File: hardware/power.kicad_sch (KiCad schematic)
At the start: 26 parts, among them J2 +, J3 -, U1 INA186A3, U2 TPS61022, U4 LP5912-3.3

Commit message: Preserve owner schematic and board before final design review
Snapshot of the saved working design supplied for review.
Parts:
- removed C1, C2: 22uF, lib:C_0603_1608Metric_L, symbol Device:C
- removed R1: 0.5mR 2W, lib:R_1206_Kelvin_4Pad_NetTie_HCS1206_L, symbol lib:R_Shunt_Kelvin
- added R2: 0.5mR 2W, lib:R_1206_Kelvin_4Pad_NetTie_HCS1206_L, symbol lib:R_Shunt_Kelvin
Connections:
- net +BATT: now also R2.4
- net CSA+: now also R2.1
- net SHUNT_SENSE_N: now also R2.3
- net SHUNT_SENSE_P: now also R2.2

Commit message: Correct Whoop schematic and prepare component library for routing
Add local BMI270 bypassing, improve regulator capacitance margin, isolate
bidirectional DShot supply domains, and correct PA reference accuracy.
Remove Q28/R11 with matching firmware polarity and retain the proven
OpenFC-Lite OSD topology. Correct the receiver LED bypass rail.

Synchronize PCB connectivity, verify component pins and land patterns,
and provide firmware bindings plus placement/layer guidance. Replace stale
manual BOM and interface plans with schematic-derived exports.

Validation: ERC 0, seven netlist checks, 48 footprint checks, 22 rule
behavior cases, and PCB schematic parity 0. The parked PCB retains layout
DRC findings and 499 unconnected items; no manufacturing or flight release.
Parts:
- removed R11: 2.4k, lib:R_0201_0603Metric_L, symbol Device:R
- added D11: MS2A40LDF, lib:DFN1610-2_L1.6-W1.0-P1.05-RD, symbol lib:MS2A40LDF
- C14: value 1uF -> 4.7uF; LCSC C76935 -> C335103; MPN GRM033R61A105ME44D -> GRM035R60J475ME15D
- U4: value LP5912-3.3 -> TLV75733; symbol lib:LP5912-3.3DRVR -> lib:TLV75733PDRVR; LCSC C524780 -> C2868428; MPN LP5912-3.3DRVR -> TLV75733PDRVR
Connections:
- net +3.3V: now also D11.2 (A)
- net +5V: now also D11.1 (K)
- net GND: now also U4.3 (GND); no longer U4.5 (GND)
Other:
- note added: "LDO REVERSE-CURRENT BYPASS"
- note removed: "HD_EN PULL-DOWN"

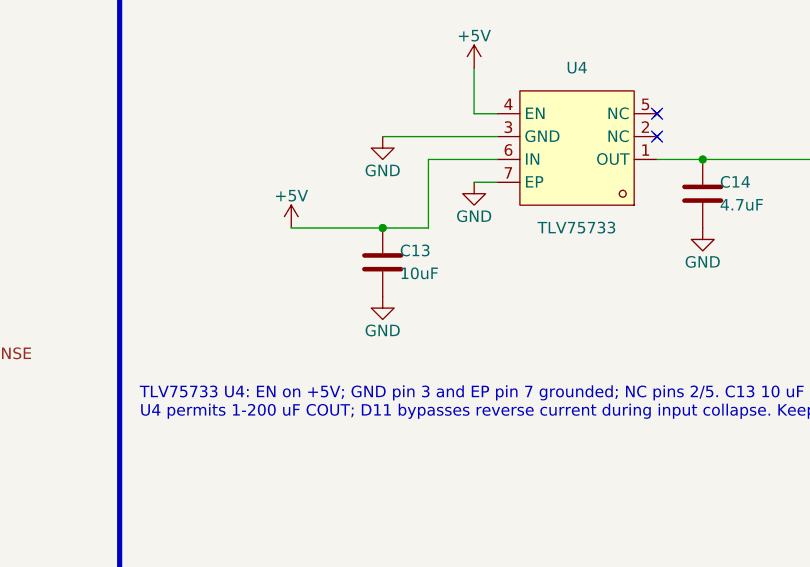
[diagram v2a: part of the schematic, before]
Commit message: Preserve owner schematic and placement edits before GPIO remap
Retain the saved layout, OSD bypass addition and component removals exactly
as received. This snapshot separates owner changes from the GPIO remap.
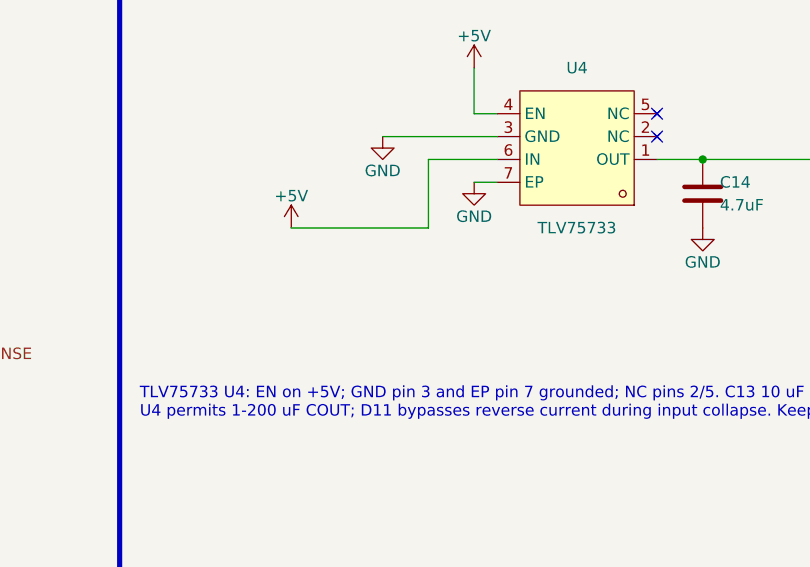
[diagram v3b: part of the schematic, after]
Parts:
- removed C13: 10uF, lib:C_0402_1005Metric_L, symbol Device:C
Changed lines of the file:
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@@
 	)
 	(junction
-		(at 283.21 46.99)
-		(diameter 0)
-		(color 0 0 0 0)
-	)
-	(junction
 		(at 45.72 124.46)
 		(diameter 0)
@@
 	)
 	(symbol
-		(lib_id "Device:C")
-		(at 283.21 50.8 0)
-		(unit 1)
-		(body_style 1)
-		(exclude_from_sim no)
-		(in_bom yes)
-		(on_board yes)
-		(in_pos_files yes)
-		(dnp no)
-		(property "Reference" "C13"
-			(at 285.115 49.53 0)
-			(show_name no)
-			(do_not_autoplace no)
-			(effects
-				(font
-					(size 1.27 1.27)
-				)
-				(justify left)
-			)
-		)
-		(property "Value" "10uF"
-			(at 285.115 52.07 0)
-			(show_name no)
-			(do_not_autoplace no)
-			(effects
-				(font
-					(size 1.27 1.27)
-				)
-				(justify left)
-			)
-		)
-		(property "Footprint" "lib:C_0402_1005Metric_L"
-			(at 283.21 50.8 0)
-			(hide yes)
-			(show_name no)
-			(do_not_autoplace no)
-			(effects
-				(font
-					(size 1.27 1.27)
-				)
-			)
-		)
-		(property "Datasheet" ""
-			(at 283.21 50.8 0)
-			(hide yes)
-			(show_name no)
-			(do_not_autoplace no)
-			(effects
-				(font
-					(size 1.27 1.27)
-				)
-			)
-		)
-		(property "Description" "Unpolarized capacitor"
-			(at 283.21 50.8 0)
-			(hide yes)
-			(show_name no)
-			(do_not_autoplace no)
-			(effects
-				(font
-					(size 1.27 1.27)
-				)
-			)
-		)
-		(property "LCSC" "C237279"
-			(at 283.21 50.8 0)
-			(hide yes)
-			(show_name no)
-			(do_not_autoplace no)
-			(effects
-				(font
-					(size 1.27 1.27)
-				)
-			)
-		)
-		(property "MPN" "GRM155C80J106ME11D"
-			(at 283.21 50.8 0)
-			(hide yes)
-			(show_name no)
-			(do_not_autoplace no)
-			(effects
-				(font
-					(size 1.27 1.27)
-				)
-			)
-		)
-		(property "Manufacturer" "Murata"
-			(at 283.21 50.8 0)
-			(hide yes)
-			(show_name no)
-			(do_not_autoplace no)
-			(effects
-				(font
-					(size 1.27 1.27)
-				)
-			)
-		)
-		(pin "1"
-		)
-		(pin "2"
-		)
-		(instances
-			(project "OpenAIO-Whoop"
-				(path "/2c3a7206-1e66-4d43-a02f-491225e20dd6/41417550-e292-5308-8e83-617f301e47b8"
-					(reference "C13")
-					(unit 1)
-				)
-			)
-		)
-	)
-	(symbol
 		(lib_id "power:+5V")
 		(at 218.44 116.84 0)
@@
 					(unit 1)
 				)
-			)
-		)
-	)
-	(symbol
-		(lib_id "power:GND")
-		(at 283.21 54.61 0)
-		(unit 1)
-		(body_style 1)
-		(exclude_from_sim no)
-		(in_bom no)
-		(on_board yes)
-		(in_pos_files no)
-		(dnp no)
-		(property "Reference" "#PWR15"
-			(at 283.21 60.96 0)
-			(hide yes)
-			(show_name no)
-			(do_not_autoplace no)
-			(effects
-				(font
-					(size 1.27 1.27)
-				)
-			)
-		)
-		(property "Value" "GND"
-			(at 283.21 58.42 0)
-			(show_name no)
-			(do_not_autoplace no)
-			(effects
-				(font
-					(size 1.27 1.27)
-				)
-			)
-		)
-		(property "Footprint" ""
-			(at 283.21 54.61 0)
-			(hide yes)
-			(show_name no)
-			(do_not_autoplace no)
-			(effects
-				(font
-					(size 1.27 1.27)
-				)
-			)
-		)
-		(property "Datasheet" ""
-			(at 283.21 54.61 0)
-			(hide yes)
-			(show_name no)
-			(do_not_autoplace no)
-			(effects
-				(font
-					(size 1.27 1.27)
-				)
-			)
-		)
-		(property "Description" "Power symbol creates a global label with name \"GND\" , ground"
-			(at 283.21 54.61 0)
-			(hide yes)
-			(show_name no)
-			(do_not_autoplace no)
-			(effects
-				(font
-					(size 1.27 1.27)
-				)
-			)
-		)
-		(pin "1"
-		)
-		(instances
-			(project "OpenAIO-Whoop"
-				(path "/2c3a7206-1e66-4d43-a02f-491225e20dd6/41417550-e292-5308-8e83-617f301e47b8"
-					(reference "#PWR15")
-					(unit 1)
-				)
